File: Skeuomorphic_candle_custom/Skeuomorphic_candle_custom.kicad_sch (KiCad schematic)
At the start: 23 parts, among them J2 Conn_01x03_Pin, Q1 SI2302, U1 ETA1061xxx

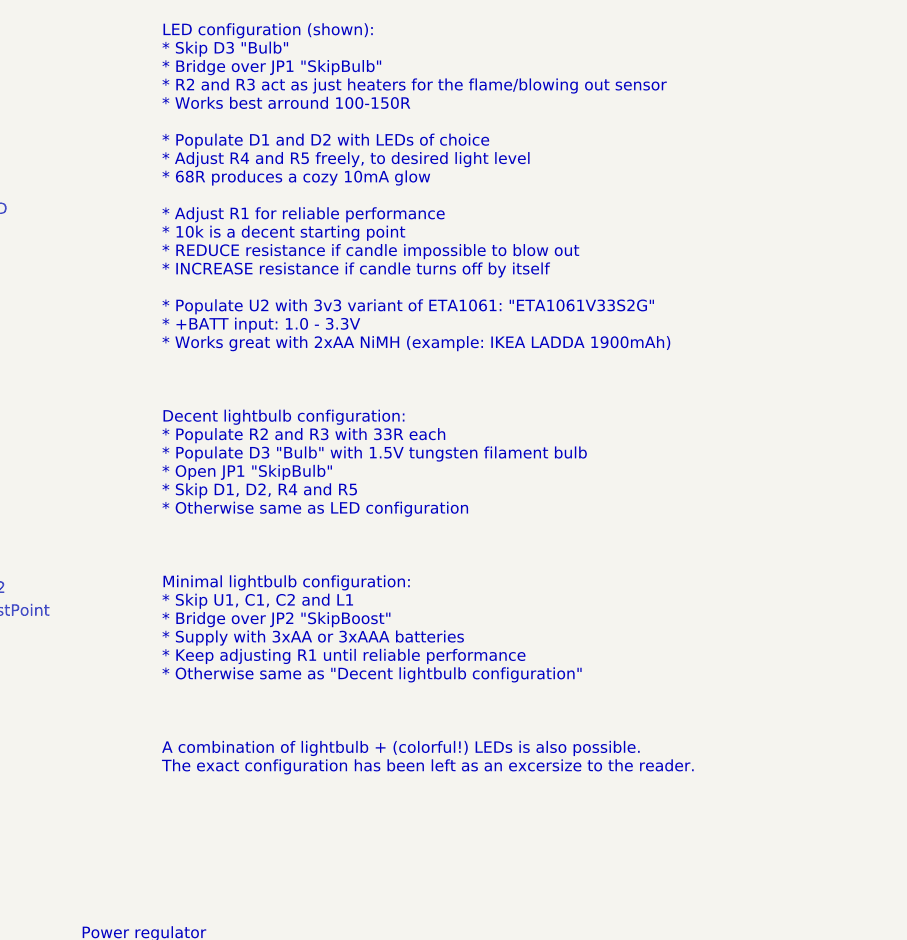
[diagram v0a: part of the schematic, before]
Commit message: added readme per pcb variant. fixed some component values
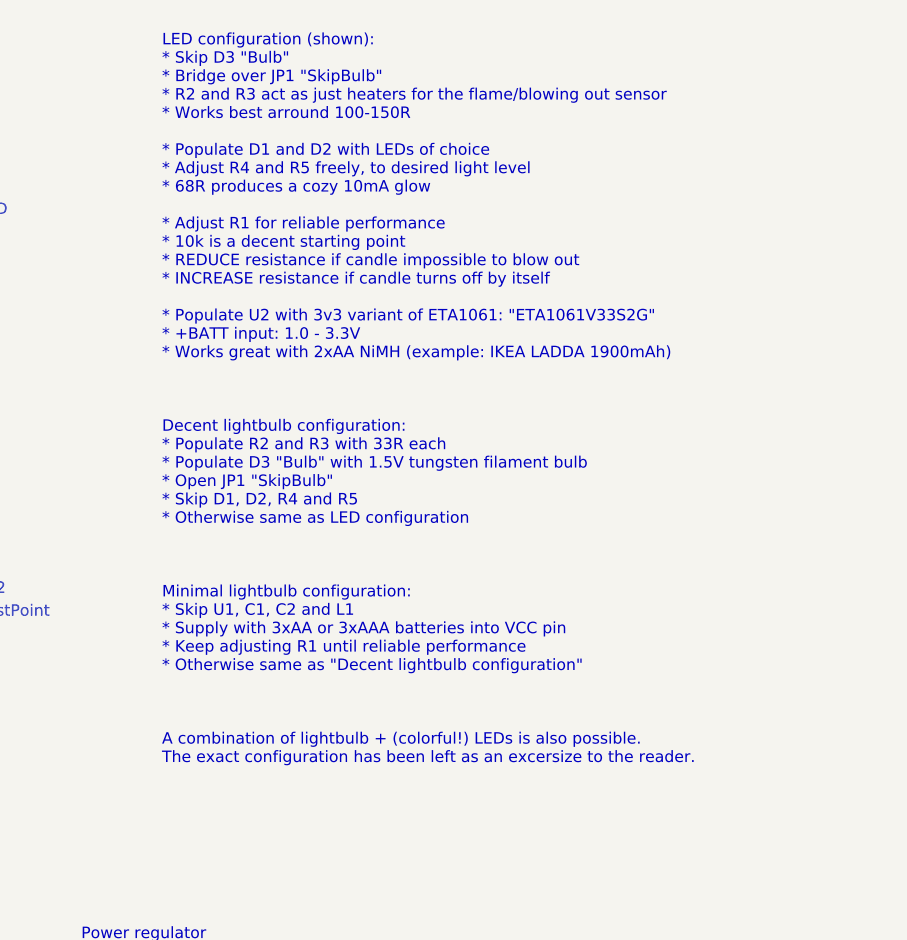
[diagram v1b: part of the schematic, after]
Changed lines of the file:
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@@
 		)
 	)
-	(text "LED configuration (shown):\n* Skip D3 \"Bulb\"\n* Bridge over JP1 \"SkipBulb\"\n* R2 and R3 act as just heaters for the flame/blowing out sensor\n* Works best arround 100-150R\n\n* Populate D1 and D2 with LEDs of choice\n* Adjust R4 and R5 freely, to desired light level\n* 68R produces a cozy 10mA glow\n\n* Adjust R1 for reliable performance\n* 10k is a decent starting point\n* REDUCE resistance if candle impossible to blow out\n* INCREASE resistance if candle turns off by itself\n\n* Populate U2 with 3v3 variant of ETA1061: \"ETA1061V33S2G\"\n* +BATT input: 1.0 - 3.3V\n* Works great with 2xAA NiMH (example: IKEA LADDA 1900mAh)\n\n\n\nDecent lightbulb configuration:\n* Populate R2 and R3 with 33R each\n* Populate D3 \"Bulb\" with 1.5V tungsten filament bulb\n* Open JP1 \"SkipBulb\"\n* Skip D1, D2, R4 and R5\n* Otherwise same as LED configuration\n\n\n\nMinimal lightbulb configuration:\n* Skip U1, C1, C2 and L1\n* Bridge over JP2 \"SkipBoost\"\n* Supply with 3xAA or 3xAAA batteries\n* Keep adjusting R1 until reliable performance\n* Otherwise same as \"Decent lightbulb configuration\"\n\n\n\nA combination of lightbulb + (colorful!) LEDs is also possible.\nThe exact configuration has been left as an excersize to the reader."
+	(text "LED configuration (shown):\n* Skip D3 \"Bulb\"\n* Bridge over JP1 \"SkipBulb\"\n* R2 and R3 act as just heaters for the flame/blowing out sensor\n* Works best arround 100-150R\n\n* Populate D1 and D2 with LEDs of choice\n* Adjust R4 and R5 freely, to desired light level\n* 68R produces a cozy 10mA glow\n\n* Adjust R1 for reliable performance\n* 10k is a decent starting point\n* REDUCE resistance if candle impossible to blow out\n* INCREASE resistance if candle turns off by itself\n\n* Populate U2 with 3v3 variant of ETA1061: \"ETA1061V33S2G\"\n* +BATT input: 1.0 - 3.3V\n* Works great with 2xAA NiMH (example: IKEA LADDA 1900mAh)\n\n\n\nDecent lightbulb configuration:\n* Populate R2 and R3 with 33R each\n* Populate D3 \"Bulb\" with 1.5V tungsten filament bulb\n* Open JP1 \"SkipBulb\"\n* Skip D1, D2, R4 and R5\n* Otherwise same as LED configuration\n\n\n\nMinimal lightbulb configuration:\n* Skip U1, C1, C2 and L1\n* Supply with 3xAA or 3xAAA batteries into VCC pin\n* Keep adjusting R1 until reliable performance\n* Otherwise same as \"Decent lightbulb configuration\"\n\n\n\nA combination of lightbulb + (colorful!) LEDs is also possible.\nThe exact configuration has been left as an excersize to the reader."
 		(exclude_from_sim no)
 		(at 120.904 71.12 0)
